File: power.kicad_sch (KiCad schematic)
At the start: 34 parts, among them J20 Conn_01x02_Pin, J21 Conn_01x02_Pin, J8 UJC-HP-L-G-5-MSMT-TR, U2 TPS2117DRLR, U3 INA260AIPW, U4 AZ1117IH-3.3TRG1

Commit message: Finalized Footprints
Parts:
- C17, C18, C19, C20, C21, C5: footprint Capacitor_SMD:C_0805_2012Metric_Pad1.18x1.45mm_HandSolder -> Capacitor_SMD:C_0603_1608Metric_Pad1.08x0.95mm_HandSolder
- R12, R13, R14, R15, R16, R18, R21, R22, R6: footprint Resistor_SMD:R_0805_2012Metric_Pad1.20x1.40mm_HandSolder -> Resistor_SMD:R_0603_1608Metric_Pad0.98x0.95mm_HandSolder
- TP1, TP2, TP3: footprint (none) -> TestPoint:TestPoint_Pad_D3.0mm
- U4: footprint (none) -> AZ1117IH_3_3TRG1:SOT223_AZ1117I_6P5X3P5_DIO-M
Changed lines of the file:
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@@
 			)
 		)
-		(property "Footprint" "Capacitor_SMD:C_0805_2012Metric_Pad1.18x1.45mm_HandSolder"
+		(property "Footprint" "Capacitor_SMD:C_0603_1608Metric_Pad1.08x0.95mm_HandSolder"
 			(at 121.6152 69.85 0)
 			(effects
@@
 			)
 		)
-		(property "Footprint" "Capacitor_SMD:C_0805_2012Metric_Pad1.18x1.45mm_HandSolder"
+		(property "Footprint" "Capacitor_SMD:C_0603_1608Metric_Pad1.08x0.95mm_HandSolder"
 			(at 50.4952 161.29 0)
 			(effects
@@
 			)
 		)
-		(property "Footprint" ""
+		(property "Footprint" "TestPoint:TestPoint_Pad_D3.0mm"
 			(at 27.94 88.9 0)
 			(effects
@@
 			)
 		)
-		(property "Footprint" "Resistor_SMD:R_0805_2012Metric_Pad1.20x1.40mm_HandSolder"
+		(property "Footprint" "Resistor_SMD:R_0603_1608Metric_Pad0.98x0.95mm_HandSolder"
 			(at 143.764 160.274 90)
 			(effects
@@
 			)
 		)
-		(property "Footprint" "Resistor_SMD:R_0805_2012Metric_Pad1.20x1.40mm_HandSolder"
+		(property "Footprint" "Resistor_SMD:R_0603_1608Metric_Pad0.98x0.95mm_HandSolder"
 			(at 143.764 133.604 90)
 			(effects
@@
 			)
 		)
-		(property "Footprint" "Resistor_SMD:R_0805_2012Metric_Pad1.20x1.40mm_HandSolder"
+		(property "Footprint" "Resistor_SMD:R_0603_1608Metric_Pad0.98x0.95mm_HandSolder"
 			(at 103.886 48.514 90)
 			(effects
@@
 			)
 		)
-		(property "Footprint" "Resistor_SMD:R_0805_2012Metric_Pad1.20x1.40mm_HandSolder"
+		(property "Footprint" "Resistor_SMD:R_0603_1608Metric_Pad0.98x0.95mm_HandSolder"
 			(at 103.886 38.354 90)
 			(effects
@@
 			)
 		)
-		(property "Footprint" "Resistor_SMD:R_0805_2012Metric_Pad1.20x1.40mm_HandSolder"
+		(property "Footprint" "Resistor_SMD:R_0603_1608Metric_Pad0.98x0.95mm_HandSolder"
 			(at 162.814 42.164 90)
 			(effects
@@
 			)
 		)
-		(property "Footprint" "Resistor_SMD:R_0805_2012Metric_Pad1.20x1.40mm_HandSolder"
+		(property "Footprint" "Resistor_SMD:R_0603_1608Metric_Pad0.98x0.95mm_HandSolder"
 			(at 154.686 49.784 90)
 			(effects
@@
 			)
 		)
-		(property "Footprint" "Capacitor_SMD:C_0805_2012Metric_Pad1.18x1.45mm_HandSolder"
+		(property "Footprint" "Capacitor_SMD:C_0603_1608Metric_Pad1.08x0.95mm_HandSolder"
 			(at 50.4952 187.96 0)
 			(effects
@@
 			)
 		)
-		(property "Footprint" "Resistor_SMD:R_0805_2012Metric_Pad1.20x1.40mm_HandSolder"
+		(property "Footprint" "Resistor_SMD:R_0603_1608Metric_Pad0.98x0.95mm_HandSolder"
 			(at 143.764 185.674 90)
 			(effects
@@
 			)
 		)
-		(property "Footprint" "Capacitor_SMD:C_0805_2012Metric_Pad1.18x1.45mm_HandSolder"
+		(property "Footprint" "Capacitor_SMD:C_0603_1608Metric_Pad1.08x0.95mm_HandSolder"
 			(at 219.4052 50.8 0)
 			(effects
@@
 			)
 		)
-		(property "Footprint" ""
+		(property "Footprint" "AZ1117IH_3_3TRG1:SOT223_AZ1117I_6P5X3P5_DIO-M"
 			(at 240.538 70.866 0)
 			(effects
@@
 			)
 		)
-		(property "Footprint" ""
+		(property "Footprint" "TestPoint:TestPoint_Pad_D3.0mm"
 			(at 27.94 100.33 0)
 			(effects
@@
 			)
 		)
-		(property "Footprint" "Capacitor_SMD:C_0805_2012Metric_Pad1.18x1.45mm_HandSolder"
+		(property "Footprint" "Capacitor_SMD:C_0603_1608Metric_Pad1.08x0.95mm_HandSolder"
 			(at 90.4748 35.56 0)
 			(effects
@@
 			)
 		)
-		(property "Footprint" "Capacitor_SMD:C_0805_2012Metric_Pad1.18x1.45mm_HandSolder"
+		(property "Footprint" "Capacitor_SMD:C_0603_1608Metric_Pad1.08x0.95mm_HandSolder"
 			(at 270.2052 49.53 0)
 			(effects
@@
 			)
 		)
-		(property "Footprint" "Resistor_SMD:R_0805_2012Metric_Pad1.20x1.40mm_HandSolder"
+		(property "Footprint" "Resistor_SMD:R_0603_1608Metric_Pad0.98x0.95mm_HandSolder"
 			(at 143.764 172.974 90)
 			(effects
@@
 			)
 		)
-		(property "Footprint" ""
+		(property "Footprint" "TestPoint:TestPoint_Pad_D3.0mm"
 			(at 27.94 110.49 0)
 			(effects
@@
 			)
 		)
-		(property "Footprint" "Resistor_SMD:R_0805_2012Metric_Pad1.20x1.40mm_HandSolder"
+		(property "Footprint" "Resistor_SMD:R_0603_1608Metric_Pad0.98x0.95mm_HandSolder"
 			(at 143.764 147.574 90)
 			(effects

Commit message: Routing
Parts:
- removed J21: Conn_01x02_Pin, Connector_PinHeader_2.54mm:PinHeader_1x02_P2.54mm_Vertical, symbol Connector:Conn_01x02_Pin
- R16: value 240 -> 100
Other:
- moved on the sheet: J20

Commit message: Bruh
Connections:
- net Vs: now also U4.4 (VOUT)
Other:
- moved on the sheet: C21

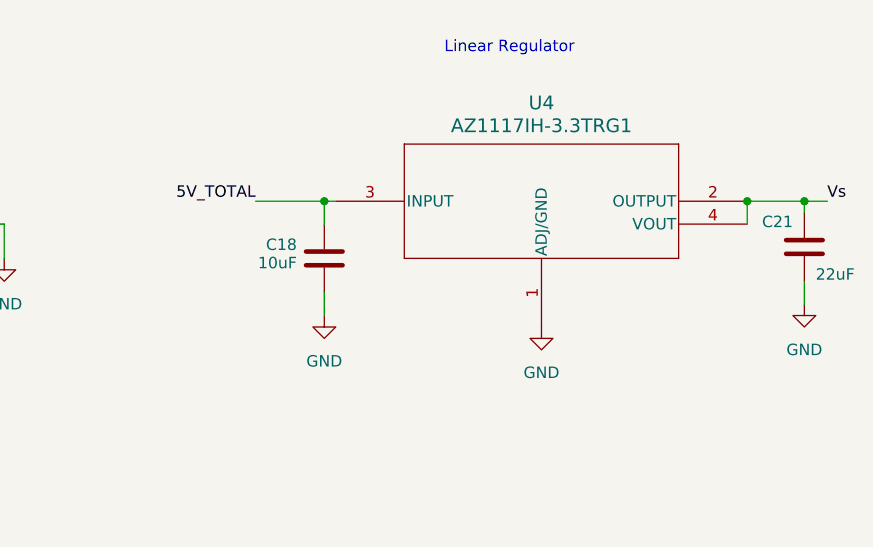
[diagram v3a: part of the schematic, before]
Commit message: Unconnected Fix
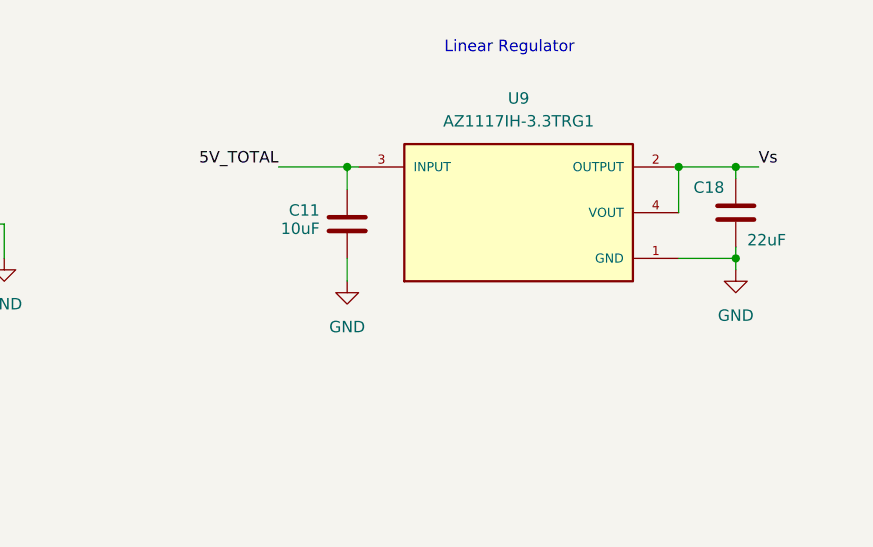
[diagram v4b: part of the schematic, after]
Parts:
- removed C21: 22uF, Capacitor_SMD:C_0603_1608Metric_Pad1.08x0.95mm_HandSolder, symbol Device:C
- removed U4: AZ1117IH-3.3TRG1, AZ1117IH_3_3TRG1:SOT223_AZ1117I_6P5X3P5_DIO-M, symbol AZ1117IH_3_3TRG1:AZ1117IH-3.3TRG1
- added C11: 10uF, Capacitor_SMD:C_0603_1608Metric_Pad1.08x0.95mm_HandSolder, symbol Device:C
- added U9: AZ1117IH-3.3TRG1, AZ1117IH-3.3TRG1:SOT230P700X185-4N, symbol AZ1117IH-3.3TRG1:AZ1117IH-3.3TRG1
- C18: value 10uF -> 22uF
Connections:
- net 5V_TOTAL: now also C11.1, U9.3 (INPUT); no longer C18.1
- net GND: now also C11.2, U9.1 (GND)
- net Vs: now also C18.1, U9.2 (OUTPUT), U9.4 (VOUT)

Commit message: Pre Design Review - Reviewed DRC Errors
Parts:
- U9: footprint AZ1117IH-3.3TRG1:SOT230P700X185-4N -> AZ1117IH_3_3TRG1 (3):SOT230P700X185-4N
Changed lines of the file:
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@@
 			)
 		)
-		(property "Footprint" "AZ1117IH-3.3TRG1:SOT230P700X185-4N"
+		(property "Footprint" "AZ1117IH_3_3TRG1 (3):SOT230P700X185-4N"
 			(at 240.03 41.91 0)
 			(effects

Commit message: Hello Bruh
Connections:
- net 5V_TOTAL: now also U2.7 (VOUT__1)
- no-connect marks 3 -> 2
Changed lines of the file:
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@@
+	)
+	(junction
+		(at 146.05 33.02)
+		(diameter 0)
+		(color 0 0 0 0)
 	)
 	(junction
@@
 		(at 50.8 44.45)
 	)
-	(no_connect
-		(at 146.05 35.56)
-	)
 	(wire
 		(pts
@@
 		)
 		(stroke
+			(width 0)
+			(type default)
+		)
+	)
+	(wire
+		(pts
+			(xy 146.05 33.02) (xy 146.05 35.56)
+		)
+		(stroke

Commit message: Routing Additions
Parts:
- TP1, TP2, TP3: footprint TestPoint:TestPoint_Pad_D3.0mm -> TestPoint:TestPoint_Pad_D4.0mm
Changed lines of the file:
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@@
 			)
 		)
-		(property "Footprint" "TestPoint:TestPoint_Pad_D3.0mm"
+		(property "Footprint" "TestPoint:TestPoint_Pad_D4.0mm"
 			(at 27.94 88.9 0)
 			(effects
@@
 			)
 		)
-		(property "Footprint" "TestPoint:TestPoint_Pad_D3.0mm"
+		(property "Footprint" "TestPoint:TestPoint_Pad_D4.0mm"
 			(at 27.94 100.33 0)
 			(effects
@@
 			)
 		)
-		(property "Footprint" "TestPoint:TestPoint_Pad_D3.0mm"
+		(property "Footprint" "TestPoint:TestPoint_Pad_D4.0mm"
 			(at 27.94 110.49 0)
 			(effects
